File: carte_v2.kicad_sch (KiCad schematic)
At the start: 0 parts

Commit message: added user input + sensors
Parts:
- added J1, J3, J4, J6, J7: Conn_01x03_Socket, symbol Connector:Conn_01x03_Socket
- added J2, J5: Conn_01x04_Socket, symbol Connector:Conn_01x04_Socket
- added R1, R2, R3: R 10K, symbol Device:R
- added RV1: R_Potentiometer, Potentiometer_THT:Potentiometer_Piher_PT-15-V02_Vertical_Hole, symbol Device:R_Potentiometer
- added SW1, SW2, SW3: SW_Push_Dual, symbol Switch:SW_Push_Dual
- added U1: Arduino_Nano, Arduino:Arduino_Nano, symbol Arduino:Arduino_Nano
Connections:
- new net: R1.1, SW1.3
- new net: R2.1, SW2.3
- new net: R3.1, SW3.3
- new net +3.3V: J3.2 (Pin_2), J4.2 (Pin_2), J5.4 (Pin_4), J6.2 (Pin_2), U1.17 (3V3)
- new net +5V: J1.1 (Pin_1), J2.1 (Pin_1), RV1.1, SW1.1, SW2.1, SW3.1, U1.27 (+5V)
- new net BUZZER: J7.1 (Pin_1), U1.9 (~D6)
- new net DHT11: J2.2 (Pin_2), U1.8 (~D5)
- new net ECG: J6.1 (Pin_1), U1.5 (D2)
- new net GND: J1.2 (Pin_2), J2.4 (Pin_4), J3.1 (Pin_1), J4.3 (Pin_3), J5.1 (Pin_1), J6.3 (Pin_3), J7.3 (Pin_3), R1.2, R2.2, R3.2, RV1.3, U1.29 (GND), U1.4 (GND)
- new net MICROPHONE: J1.3 (Pin_3), U1.22 (A3/D17)
- new net POT: RV1.2, U1.26 (A7/D21)
- new net SCL_CO2: J5.2 (Pin_2), U1.24 (A5/D19)
- new net SDA_CO2: J5.3 (Pin_3), U1.23 (A4/D18)
- new net SHARP_ANALOG: J3.3 (Pin_3), U1.25 (A6/D20)
- new net SHARP_DIGITAL: J4.1 (Pin_1), U1.6 (~D3)
- new net SW1: SW1.4, U1.7 (D4)
- new net SW2: SW2.4, U1.10 (D7)
- new net SW3: SW3.4, U1.11 (D8)
- no-connect marks 0 -> 3
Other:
- note added: "BUZZER"
- note added: "CO2/VOC sensor (I2C)"
- note added: "DHT11 Temperature & Humidity"
- note added: "ECG"
- note added: "Microphone module"
- note added: "Sharp DUST Sensor (Digital)"
- note added: "Sharp DUST sensor (Analog)"
- note added: "USER INPUTS"

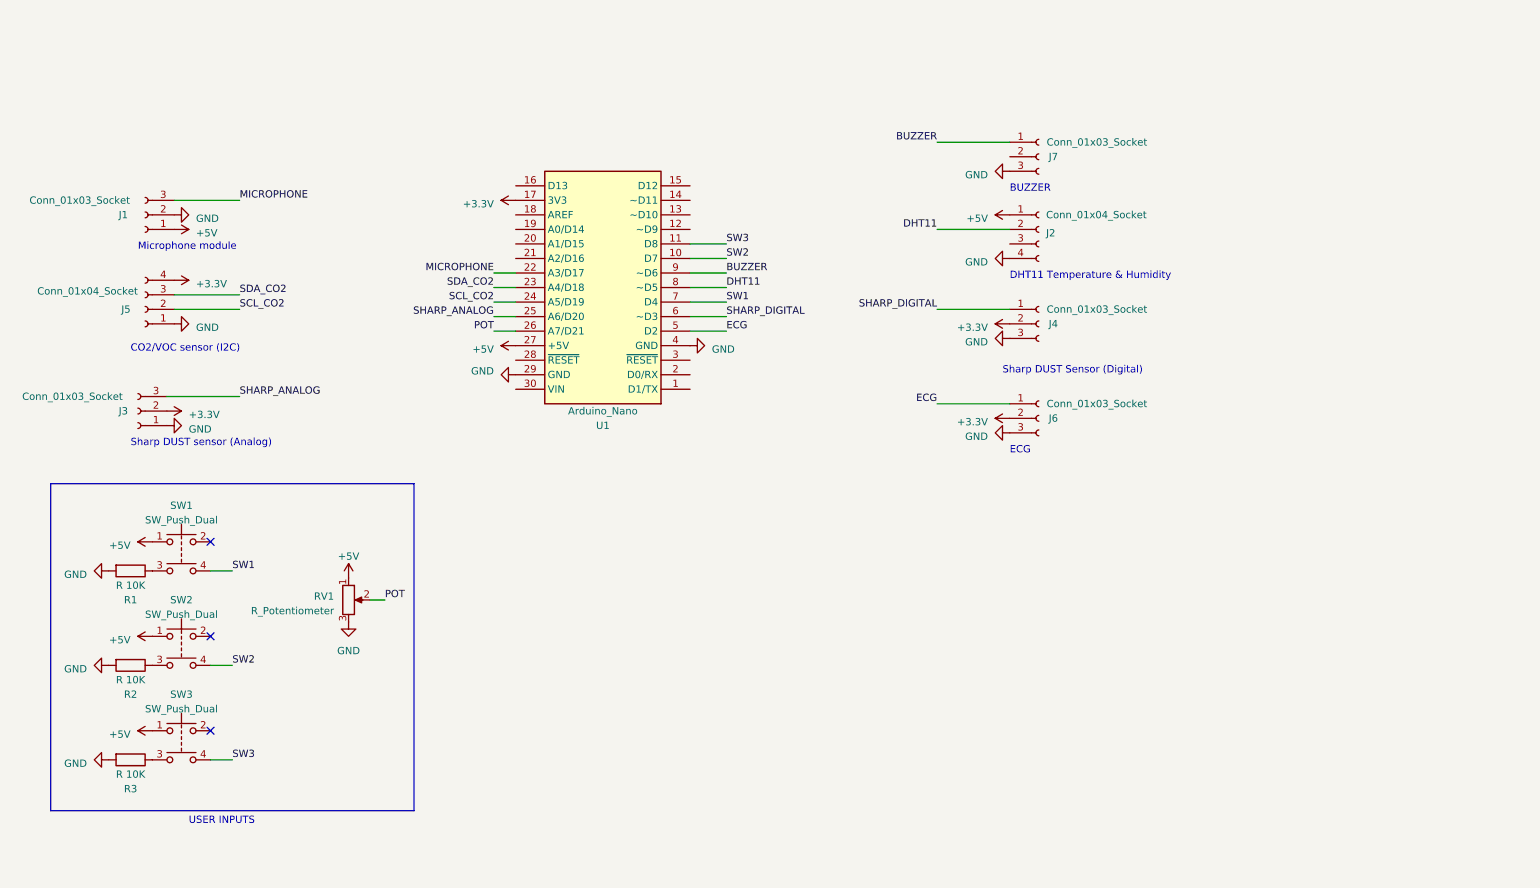
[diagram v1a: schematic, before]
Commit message: added rgb leds + reworked buzzer
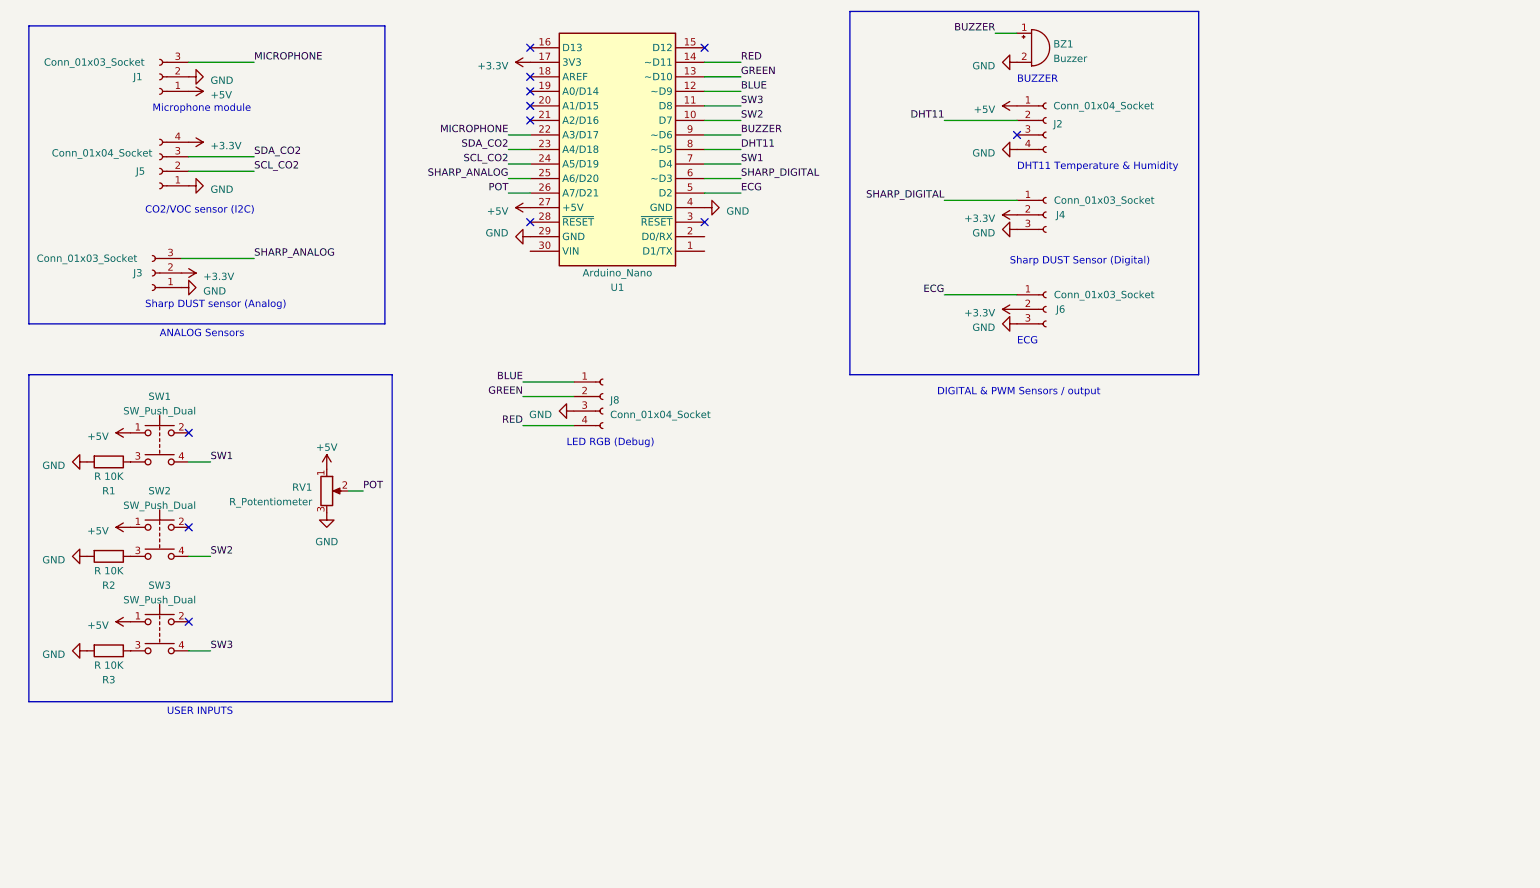
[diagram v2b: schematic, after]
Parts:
- removed J7: Conn_01x03_Socket, symbol Connector:Conn_01x03_Socket
- added BZ1: Buzzer, Buzzer_Beeper:Buzzer_12x9.5RM7.6, symbol Device:Buzzer
- added J8: Conn_01x04_Socket, symbol Connector:Conn_01x04_Socket
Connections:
- net BUZZER: now also BZ1.1 (-)
- net GND: now also BZ1.2 (+), J8.3 (Pin_3)
- net BLUE: now reaches U1.12 (~D9)
- net BLUE: now also J8.1 (Pin_1)
- net GREEN: now reaches U1.13 (~D10)
- net GREEN: now also J8.2 (Pin_2)
- net RED: now reaches U1.14 (~D11)
- net RED: now also J8.4 (Pin_4)
- no-connect marks 3 -> 12
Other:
- note added: "ANALOG Sensors"
- note added: "DIGITAL & PWM Sensors / output"
- note added: "LED RGB (Debug)"
- moved on the sheet: J1, J2, J3, J4, J5, J6, R1, R2, R3, RV1, SW1, SW2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

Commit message: added raspberry GPIO + resitor
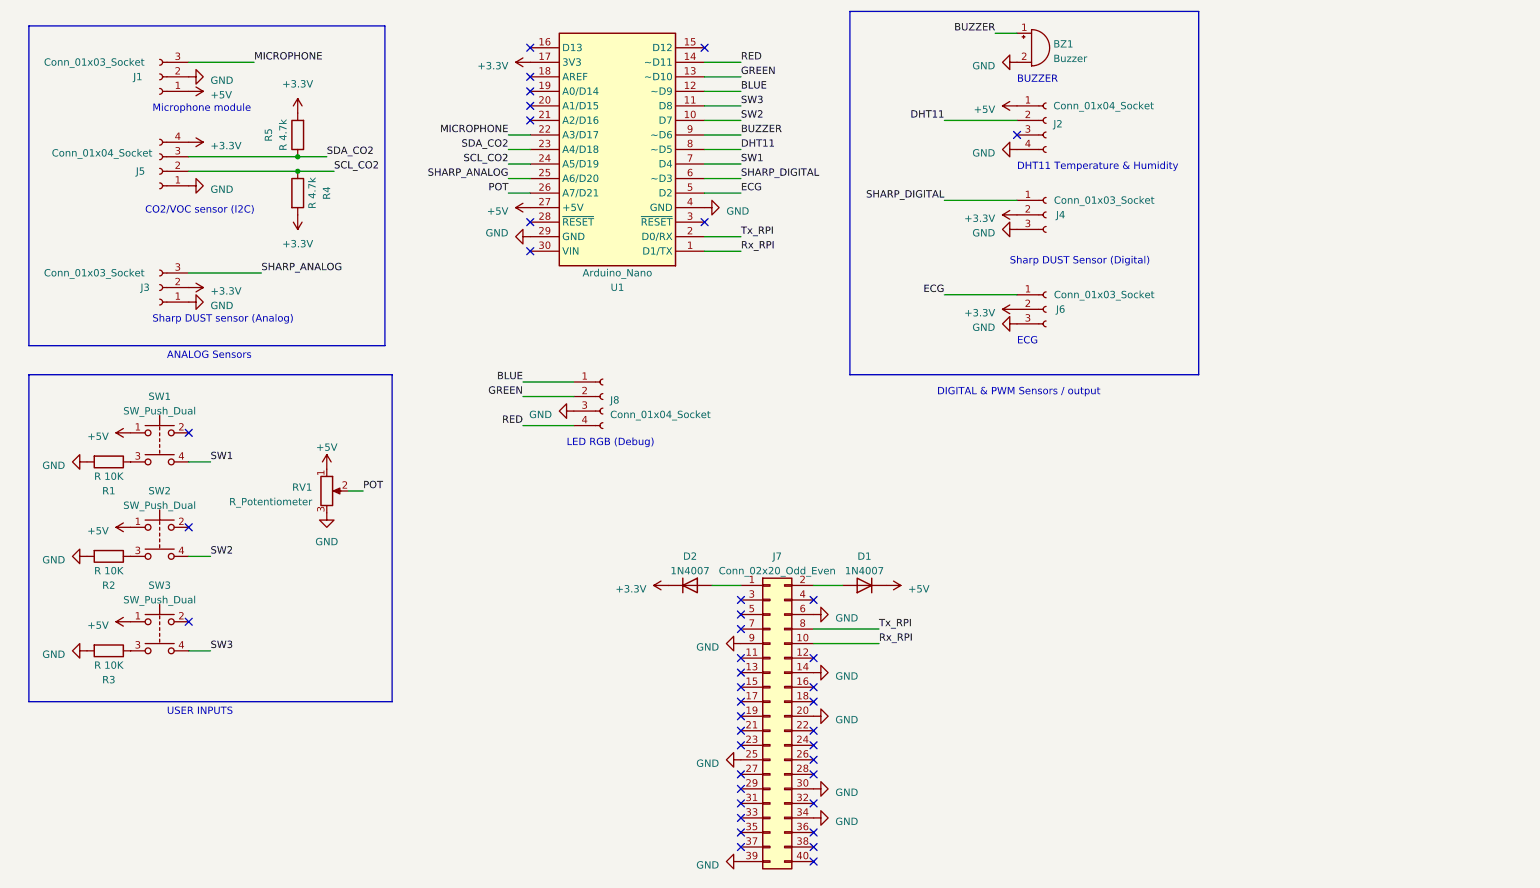
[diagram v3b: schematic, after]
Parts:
- added D1, D2: 1N4007, Diode_THT:D_DO-41_SOD81_P10.16mm_Horizontal, symbol Diode:1N4007
- added J7: Conn_02x20_Odd_Even, symbol Connector_Generic:Conn_02x20_Odd_Even
- added R4, R5: R 4.7k, symbol Device:R
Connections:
- net +3.3V: now also D2.1 (K), R4.2, R5.2
- net +5V: now also D1.1 (K)
- net GND: now also J7.14 (Pin_14), J7.20 (Pin_20), J7.25 (Pin_25), J7.30 (Pin_30), J7.34 (Pin_34), J7.39 (Pin_39), J7.6 (Pin_6), J7.9 (Pin_9)
- net SCL_CO2: now also R4.1
- net SDA_CO2: now also R5.1
- net Rx_RPI: now reaches U1.1 (D1/TX)
- net Rx_RPI: now also J7.10 (Pin_10)
- net Tx_RPI: now reaches U1.2 (D0/RX)
- net Tx_RPI: now also J7.8 (Pin_8)
- new net: D1.2 (A), J7.2 (Pin_2)
- new net: D2.2 (A), J7.1 (Pin_1)
- no-connect marks 12 -> 41
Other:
- moved on the sheet: J3

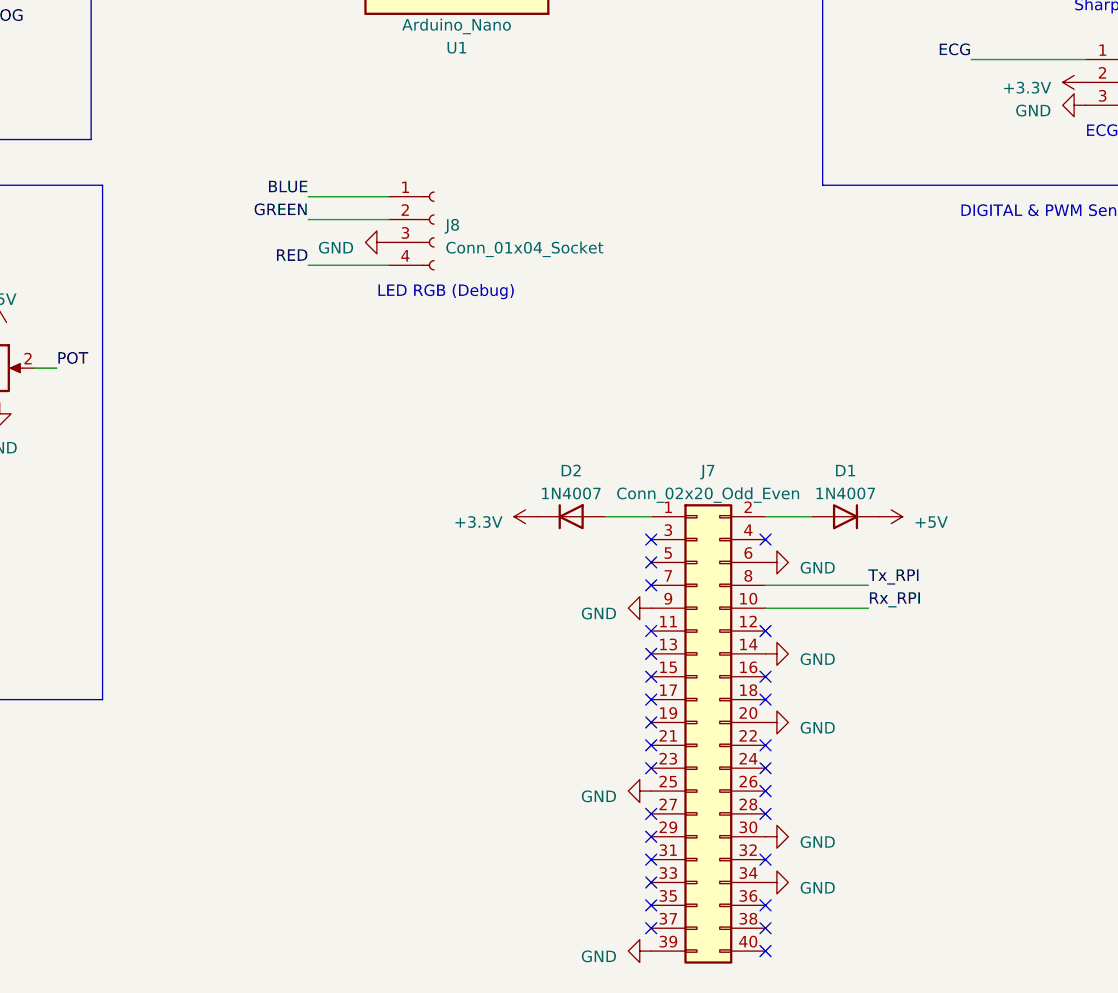
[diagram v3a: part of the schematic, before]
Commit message: added resistor + began routing
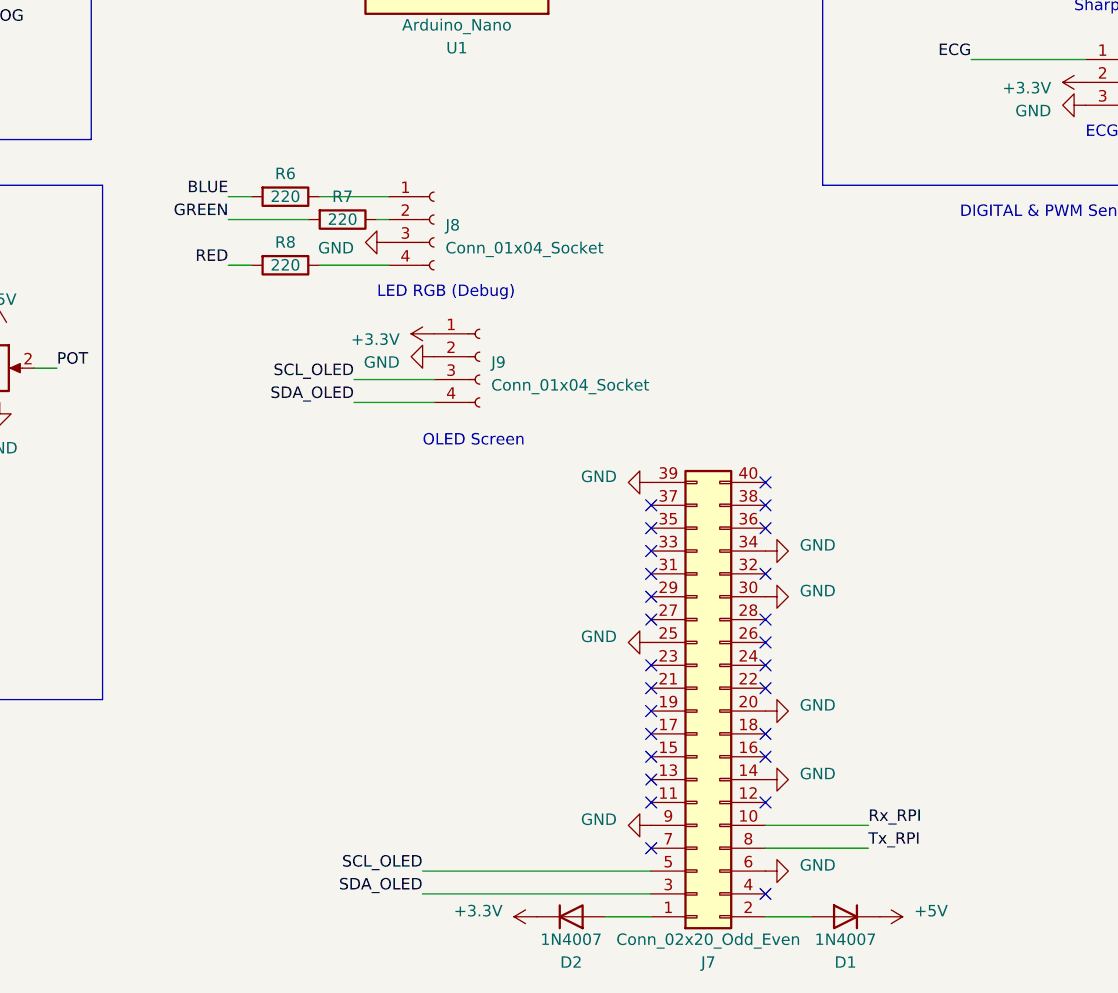
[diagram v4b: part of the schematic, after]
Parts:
- added J9: Conn_01x04_Socket, Connector_PinHeader_2.00mm:PinHeader_1x04_P2.00mm_Vertical, symbol Connector:Conn_01x04_Socket
- added R6, R7, R8: 220, Resistor_THT:R_Axial_DIN0204_L3.6mm_D1.6mm_P7.62mm_Horizontal, symbol Device:R
- BZ1: footprint Buzzer_Beeper:Buzzer_12x9.5RM7.6 -> Buzzer_Beeper:Buzzer_15x7.5RM7.6
- J1, J3, J4, J6: footprint (none) -> Connector_PinHeader_2.00mm:PinHeader_1x03_P2.00mm_Vertical
- J2, J5, J8: footprint (none) -> Connector_PinHeader_2.00mm:PinHeader_1x04_P2.00mm_Vertical
- J7: footprint (none) -> Connector_PinHeader_2.00mm:PinHeader_2x20_P2.00mm_Vertical
- R1, R2, R3, R4, R5: footprint (none) -> Resistor_THT:R_Axial_DIN0204_L3.6mm_D1.6mm_P7.62mm_Horizontal
- RV1: footprint Potentiometer_THT:Potentiometer_Piher_PT-15-V02_Vertical_Hole -> Potentiometer_THT:Potentiometer_Runtron_RM-065_Vertical
- SW1, SW2, SW3: footprint (none) -> Button_Switch_THT:SW_PUSH_6mm_H5mm
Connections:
- net +3.3V: now also J9.1 (Pin_1)
- net BLUE: now also R6.2; no longer J8.1 (Pin_1)
- net GND: now also J9.2 (Pin_2)
- net GREEN: now also R7.2; no longer J8.2 (Pin_2)
- net RED: now also R8.2; no longer J8.4 (Pin_4)
- net SDA_OLED: now reaches J7.3 (Pin_3)
- net SDA_OLED: now also J9.4 (Pin_4)
- net SCL_OLED: now reaches J7.5 (Pin_5)
- net SCL_OLED: now also J9.3 (Pin_3)
- new net: J8.2 (Pin_2), R7.1
- new net: J8.1 (Pin_1), R6.1
- new net: J8.4 (Pin_4), R8.1
- no-connect marks 41 -> 39
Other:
- note added: "OLED Screen"
- moved on the sheet: D1, D2, J7
